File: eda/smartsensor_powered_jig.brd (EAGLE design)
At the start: 47 x 26.7 mm, 12 parts, among them J2 AVR_SPI_PRG_6PTH

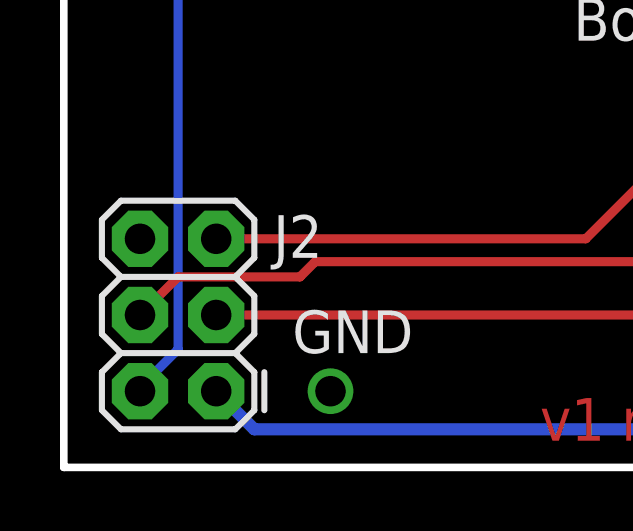
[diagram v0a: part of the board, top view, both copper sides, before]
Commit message: Ribboncable pinout fixed.
On battery_buzzer, smartsensor, and smartsensorPowered.
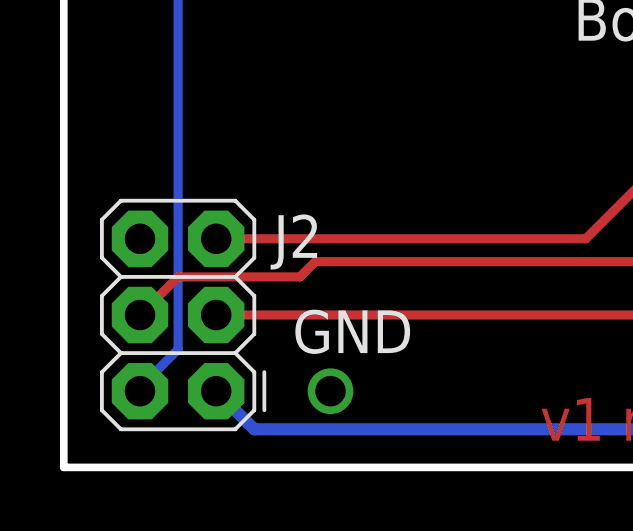
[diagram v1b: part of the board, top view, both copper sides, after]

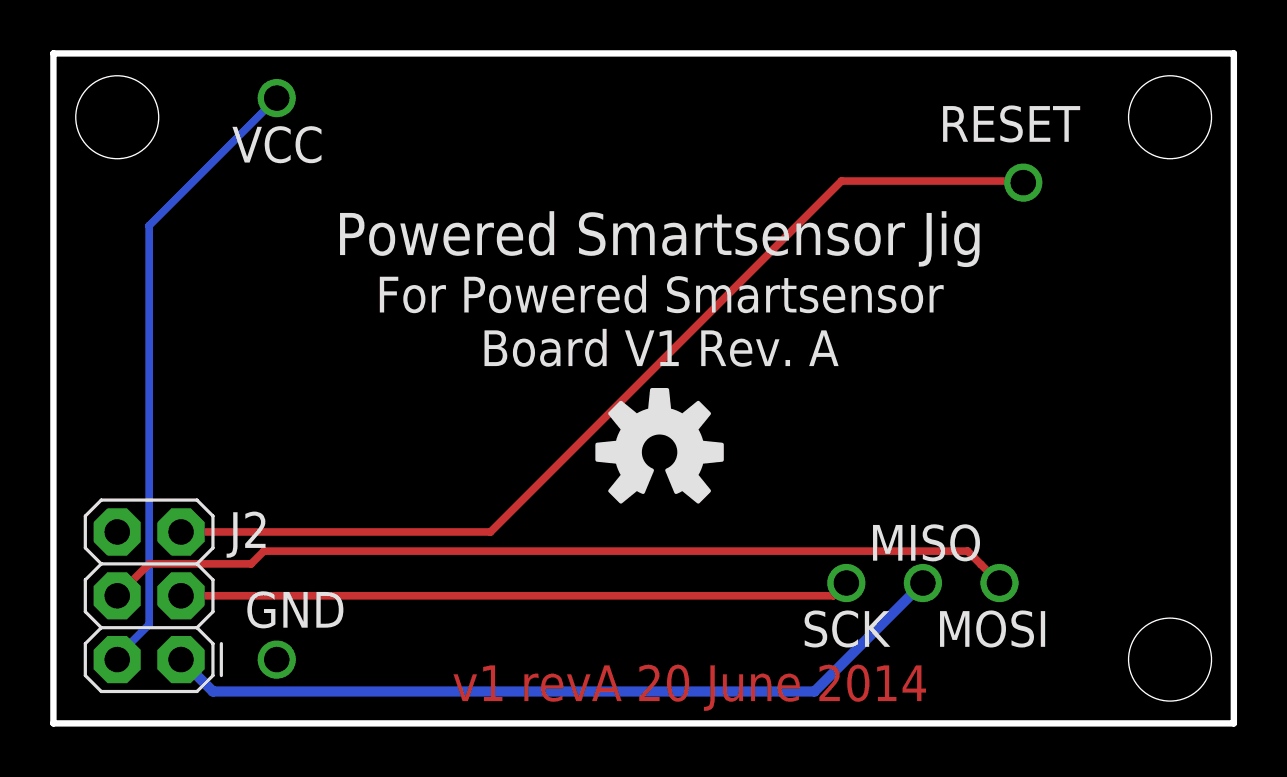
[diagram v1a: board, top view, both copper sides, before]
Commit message: All jigs probe vias accessible after populating.
Also changed "VCC" signal name on jigs to "5V" to match boards.
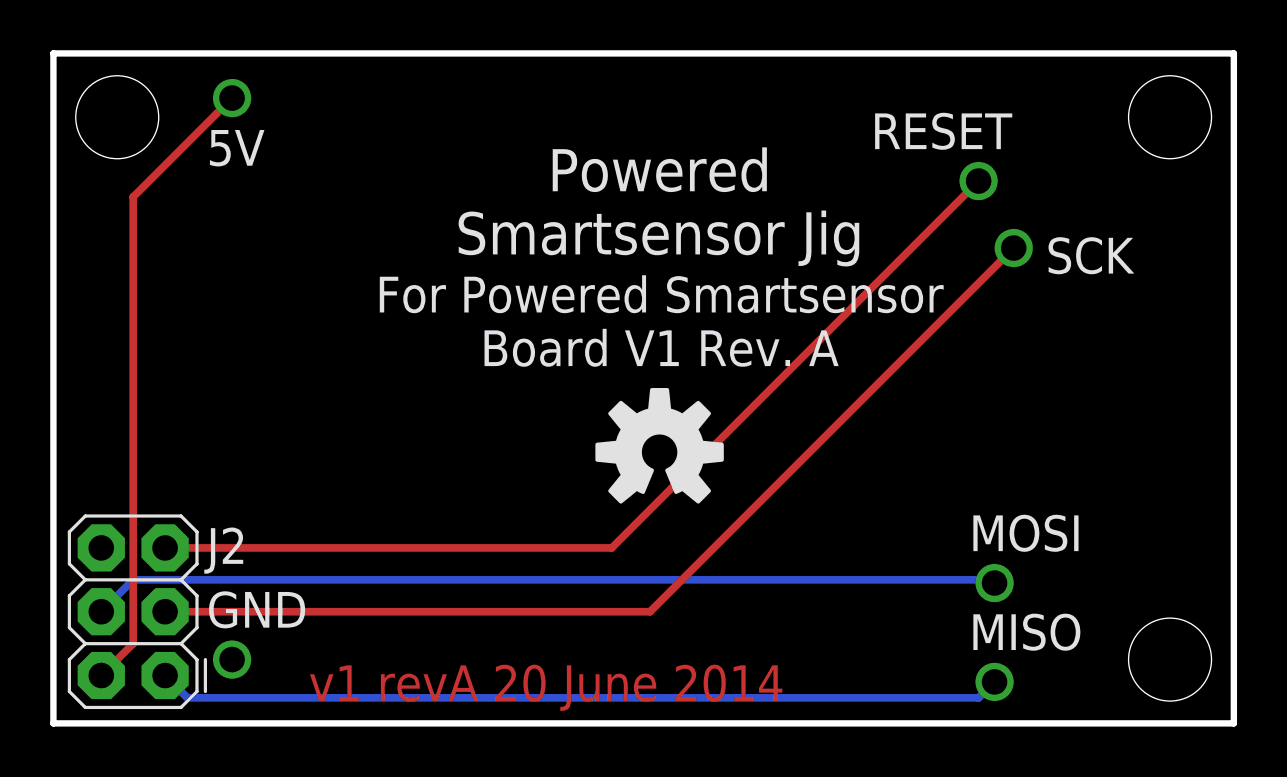
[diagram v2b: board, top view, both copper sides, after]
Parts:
- removed VCC: (no value), pie:POGO_PIN_394
- added 5V: (no value), pie:POGO_PIN_394
- moved SCK 14.9 mm to (38.2, 18.9)
- moved MISO 4.86 mm to (37.5, 1.65)
- moved RESET 1.78 mm to (36.8, 21.6)
- moved GND 1.78 mm to (7.11, 2.54)
- moved J2 0.90 mm to (4.45, 1.91)
- moved MOSI 0.20 mm to (37.5, 5.59)
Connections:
- removed net VCC: J2.2, VCC.POGO_PIN
- new net 5V: 5V.POGO_PIN, J2.2
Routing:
- net 5V: track 0.00 -> 25.1 mm
- net VCC: track 25.0 -> 0.00 mm
- net SCK: track 26.7 -> 39.8 mm
- net MISO: track 31.8 -> 33.7 mm
- net RESET: track 39.3 -> 38.4 mm
- added copper zone on layer 1, net 5V
- removed copper zone on layer 1, net GND

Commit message: Standardized copyright and "Design by" info among boards.
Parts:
- moved U$2 0.63 mm to (23.5, 5.71)
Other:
- board text added: "(c) Pioneers in Engineering. Design by: Krystyn Neisess and Vincent Donato. This design is open source hardware. For more information, visit pioneers.berkeley.edu/opensource."
- board text removed: "(c) Pioneers in Engineering Design by: Krystyn Neisess and Vincent Donato This design is open source hardware. For more information visit pioneers.berkeley.edu/opensource"
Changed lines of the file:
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@@
 <wire x1="46.99" y1="26.67" x2="0" y2="26.67" width="0.254" layer="20"/>
 <wire x1="0" y1="26.67" x2="0" y2="0" width="0.254" layer="20"/>
-<text x="34.29" y="19.685" size="0.762" layer="22" font="vector" ratio="20" rot="SMR0" align="top-left">(c) Pioneers in Engineering
-Design by:
-Krystyn Neisess and Vincent Donato
+<text x="23.495" y="18.415" size="0.889" layer="22" font="vector" ratio="15" rot="SMR0" align="top-center">(c) Pioneers in Engineering.
+Design by:  Krystyn Neisess and Vincent Donato.
 This design is open source hardware.
-For more information visit
-pioneers.berkeley.edu/opensource</text>
+For more information, visit
+pioneers.berkeley.edu/opensource.</text>
 <text x="24.13" y="22.86" size="1.6764" layer="21" font="vector" ratio="15" align="top-center">Powered
 Smartsensor Jig</text>
@@
 </element>
 <element name="U$1" library="pie" package="OSHW-LOGO-M" value="" x="24.13" y="10.795"/>
-<element name="U$2" library="pie" package="PIE-LOGO-SMALL" value="" x="24.13" y="5.715" rot="MR0"/>
+<element name="U$2" library="pie" package="PIE-LOGO-SMALL" value="" x="23.495" y="5.715" rot="MR0"/>
 <element name="U$3" library="pie" package="STAND-OFF" value="" x="44.45" y="2.54"/>
 <element name="U$4" library="pie" package="STAND-OFF" value="" x="2.54" y="24.13"/>
